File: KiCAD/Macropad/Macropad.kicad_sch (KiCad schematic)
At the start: 30 parts, among them SW1 SW_Push_45deg, SW2 SW_Push_45deg, SW3 SW_Push_45deg, SW4 SW_Push_45deg, SW5 SW_Push_45deg, SW6 SW_Push_45deg, SW7 RotaryEncoder_Switch, U1 XIAO-RP2040-DIP, U2 SSD1306

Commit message: Update layout, schematic, and interactive BOM with part numbers
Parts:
- R2: Part_Number (none) -> 56-CCF554K70FKE36CT-ND; Vendor (none) -> Digi-Key
- U1: value XIAO-RP2040-DIP -> XIAO-RP2350-DIP; Part_Number 1597-102010428-ND -> 1597-102010550-ND
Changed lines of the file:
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@@
 			)
 		)
-		(property "Value" "XIAO-RP2040-DIP"
+		(property "Value" "XIAO-RP2350-DIP"
 			(at 212.725 41.91 0)
 			(effects
@@
 			)
 		)
-		(property "Datasheet" "https://files.seeedstudio.com/wiki/XIAO-RP2040/res/rp2040_datasheet.pdf"
-			(at 210.82 39.37 0)
-			(effects
-				(font
-					(size 1.27 1.27)
-				)
-				(hide yes)
-			)
-		)
-		(property "Description" ""
+		(property "Datasheet" "https://mm.digikey.com/Volume0/opasdata/d220001/medias/docus/8932/102010550.pdf"
+			(at 210.82 39.37 0)
+			(effects
+				(font
+					(size 1.27 1.27)
+				)
+				(hide yes)
+			)
+		)
+		(property "Description" "High preformance microcontroller"
 			(at 210.82 39.37 0)
 			(effects
@@
 			)
 		)
-		(property "Part_Number" "1597-102010428-ND"
+		(property "Part_Number" "1597-102010550-ND "
 			(at 210.82 39.37 0)
 			(effects
@@
 			(at 172.72 49.53 0)
 			(effects
+				(font
+					(size 1.27 1.27)
+				)
+				(hide yes)
+			)
+		)
+		(property "Part_Number" "56-CCF554K70FKE36CT-ND"
+			(at 172.72 49.53 0)
+			(effects
+				(font
+					(size 1.27 1.27)
+				)
+				(hide yes)
+			)
+		)
+		(property "Vendor" "Digi-Key"
+			(at 172.72 49.53 0)
+			(effects

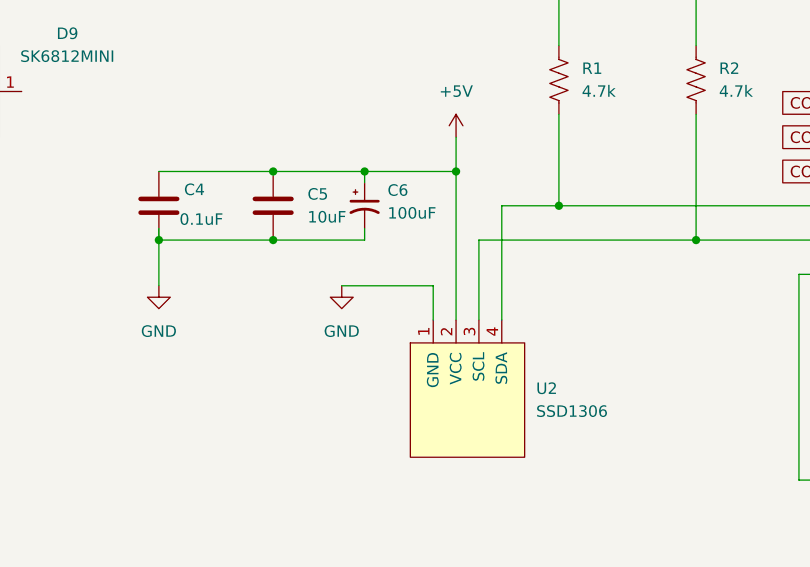
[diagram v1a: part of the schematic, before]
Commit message: Fixed a crossed wire issue and an issue with my microcontroller.
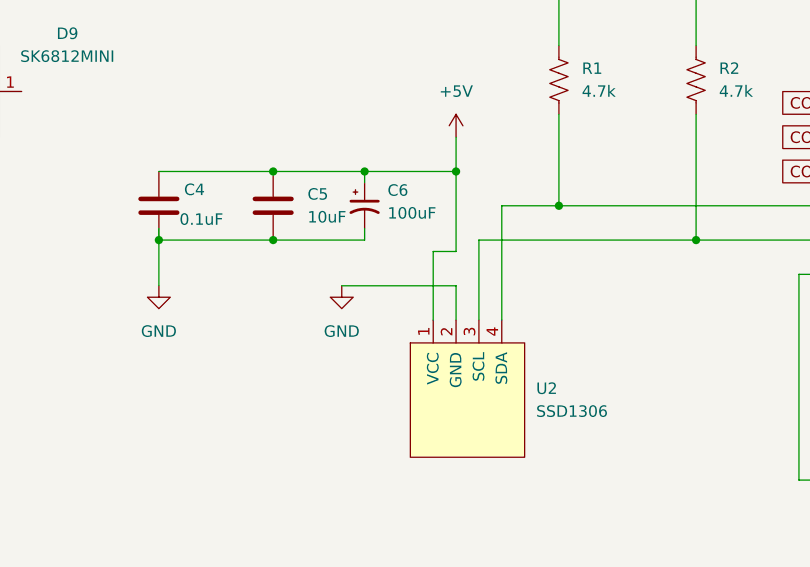
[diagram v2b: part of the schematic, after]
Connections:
- net +5V: now also U2.1 (VCC); no longer U2.2 (VCC)
- net GND: now also U2.2 (GND); no longer U2.1 (GND)
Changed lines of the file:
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@@
+	)
+	(junction
+		(at 146.05 59.69)
+		(diameter 0)
+		(color 0 0 0 0)
 	)
 	(junction
@@
 	)
 	(junction
-		(at 146.05 59.69)
-		(diameter 0)
-		(color 0 0 0 0)
-	)
-	(junction
 		(at 157.48 39.37)
 		(diameter 0)
@@
 	(wire
 		(pts
-			(xy 133.35 72.39) (xy 143.51 72.39)
+			(xy 133.35 72.39) (xy 146.05 72.39)
 		)
 		(stroke
@@
 	(wire
 		(pts
+			(xy 146.05 72.39) (xy 146.05 76.2)
+		)
+		(stroke
+			(width 0)
+			(type default)
+		)
+	)
+	(wire
+		(pts
 			(xy 52.07 182.88) (xy 81.28 182.88)
 		)
@@
 	(wire
 		(pts
+			(xy 143.51 68.58) (xy 146.05 68.58)
+		)
+		(stroke
+			(width 0)
+			(type default)
+		)
+	)
+	(wire
+		(pts
 			(xy 27.94 29.21) (xy 39.37 29.21)
 		)
@@
 	(wire
 		(pts
-			(xy 143.51 76.2) (xy 143.51 72.39)
-		)
-		(stroke
-			(width 0)
-			(type default)
-		)
-	)
-	(wire
-		(pts
 			(xy 212.09 97.79) (xy 212.09 82.55)
 		)
@@
 	(wire
 		(pts
+			(xy 143.51 76.2) (xy 143.51 68.58)
+		)
+		(stroke
+			(width 0)
+			(type default)
+		)
+	)
+	(wire
+		(pts
 			(xy 247.65 46.99) (xy 259.08 46.99)
 		)
@@
 	(wire
 		(pts
-			(xy 146.05 59.69) (xy 146.05 76.2)
-		)
-		(stroke
-			(width 0)
-			(type default)
-		)
-	)
-	(wire
-		(pts
 			(xy 80.01 144.78) (xy 106.68 144.78)
 		)
@@
 		)
 		(stroke
+			(width 0)
+			(type default)
+		)
+	)
+	(wire
+		(pts
+			(xy 146.05 68.58) (xy 146.05 59.69)
+		)
+		(stroke
